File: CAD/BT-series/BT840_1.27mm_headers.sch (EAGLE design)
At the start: 64 parts, among them J1 SM02B-SRSS-TB(LF)(SN), U1 TPD4S012DRYR, U2 BT840, U3 LP5907MFX-3.3/NOPB, U4 LP5907MFX-3.3/NOPB, U5 ADS131M08IPBS, U6 BQ24072RGTR, U7 DX4R005JJ2R1800, X1 ABM3B-8.000MHZ-B2-T, X2 FC-12M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

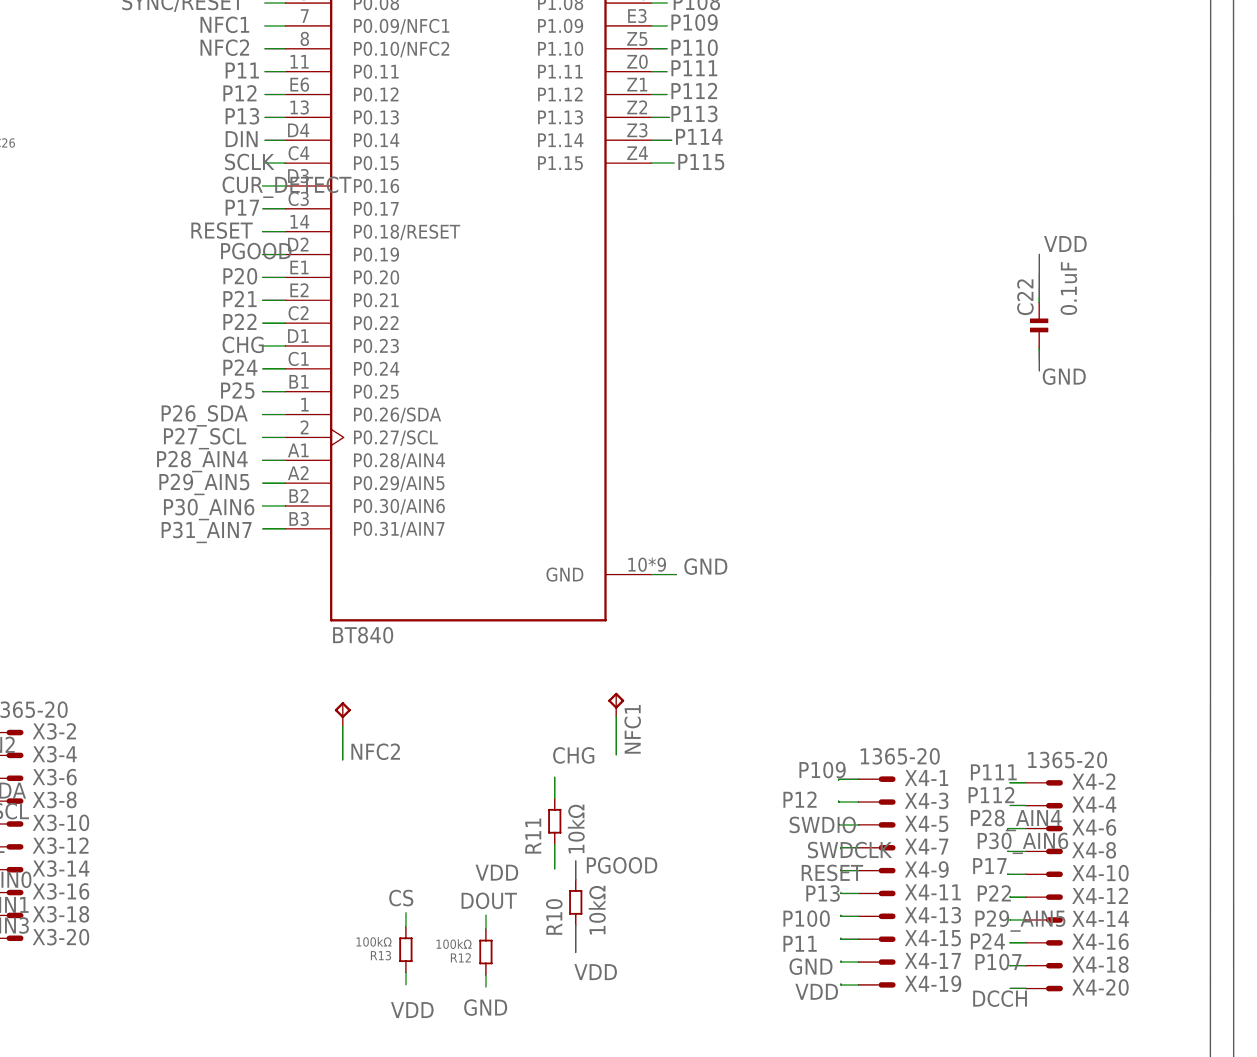
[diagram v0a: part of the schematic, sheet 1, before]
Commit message: modifed io order on bt840, some nrf52840 firmware cleanup (need to update with compass and audio too)
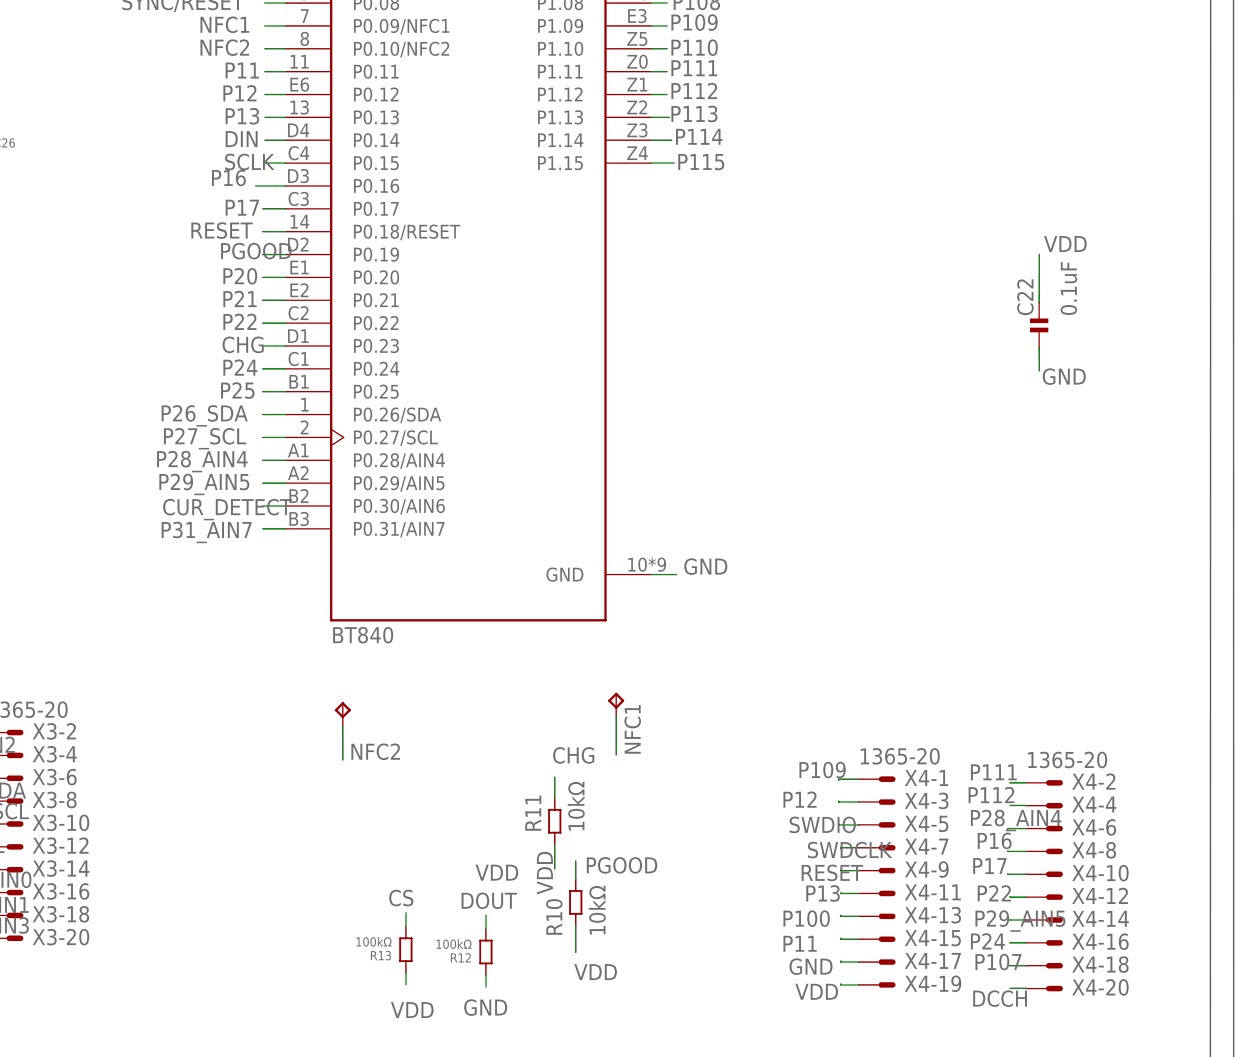
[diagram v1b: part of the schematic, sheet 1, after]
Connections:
- removed net P30_AIN6: U2.P0.30/AIN6, X4-8.S
- new net P16: U2.P0.16, X4-8.S
- net CUR_DETECT: now also U2.P0.30/AIN6; no longer U2.P0.16

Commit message: fixed cur_detect compatibility for bt40/bt840
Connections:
- removed net P29_AIN5: U2.P0.29/AIN5, X4-14.S
- new net P30_AIN6: U2.P0.30/AIN6, X4-14.S
- net CUR_DETECT: now also U2.P0.29/AIN5; no longer U2.P0.30/AIN6

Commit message: broke out the last gpio
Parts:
- added JP1: (no value), pinhead:PINHD-1X1
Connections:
- net P105: now also JP1.1
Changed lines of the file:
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@@
 <part name="X5" library="con-leotronics" library_urn="urn:adsk.eagle:library:160" deviceset="1365-16" device="" package3d_urn="urn:adsk.eagle:package:7964/1"/>
 <part name="U2" library="BT840" deviceset="BT840" device=""/>
+<part name="JP1" library="pinhead" library_urn="urn:adsk.eagle:library:325" deviceset="PINHD-1X1" device="" package3d_urn="urn:adsk.eagle:package:22485/2"/>
 </parts>
 <sheets>
@@
 <attribute name="VALUE" x="247.1419" y="68.5798" size="1.778009375" layer="96"/>
 </instance>
+<instance part="JP1" gate="G$1" x="331.724" y="147.574" smashed="yes">
+<attribute name="NAME" x="325.374" y="150.749" size="1.778" layer="95"/>
+<attribute name="VALUE" x="325.374" y="142.494" size="1.778" layer="96"/>
+</instance>
 </instances>
 <busses>
@@
 <label x="284.988" y="146.304" size="1.778" layer="95"/>
 </segment>
-</net>
+<segment>
+<pinref part="JP1" gate="G$1" pin="1"/>
+<wire x1="329.184" y1="147.574" x2="320.548" y2="147.574" width="0.1524" layer="91"/>
+<label x="316.23" y="148.082" size="1.778" layer="95"/>
+</segment>
+</net>

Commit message: update
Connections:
- removed net CLKIN: C3.1, U5.XTAL1, X1.1
- new net 8.192MHZ: C3.1, U5.XTAL1, X1.1, X3-19.S
- net CLKOUT: no longer X3-19.S
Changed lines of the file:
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@@
-</segment>
-</net>
-<net name="CLKIN" class="0">
-<segment>
-<pinref part="U5" gate="G$1" pin="XTAL1"/>
-<wire x1="439.293" y1="147.4978" x2="441.833" y2="147.4978" width="0.1524" layer="91"/>
-<label x="442.087" y="146.9898" size="1.778" layer="95"/>
-</segment>
-<segment>
-<pinref part="X1" gate="G$1" pin="1"/>
-<wire x1="481.965" y1="139.3698" x2="479.425" y2="139.3698" width="0.1524" layer="91"/>
-<label x="476.885" y="141.9098" size="1.778" layer="95"/>
-</segment>
-<segment>
-<pinref part="C3" gate="G$1" pin="1"/>
-<wire x1="471.805" y1="135.5344" x2="471.805" y2="139.3698" width="0.1524" layer="91"/>
-<label x="466.725" y="139.3698" size="1.778" layer="95"/>
 </segment>
 </net>
@@
 <label x="507.365" y="139.3698" size="1.778" layer="95"/>
 </segment>
-<segment>
-<pinref part="X3" gate="-19" pin="S"/>
-<wire x1="192.0494" y1="35.814" x2="190.5" y2="35.814" width="0.1524" layer="91"/>
-<label x="180.594" y="35.052" size="1.778" layer="95"/>
-</segment>
 </net>
 <net name="TMR" class="0">
@@
 </segment>
 </net>
+<net name="8.192MHZ" class="0">
+<segment>
+<pinref part="X3" gate="-19" pin="S"/>
+<wire x1="192.0494" y1="35.814" x2="190.5" y2="35.814" width="0.1524" layer="91"/>
+<label x="180.594" y="35.052" size="1.778" layer="95"/>
+</segment>
+<segment>
+<pinref part="U5" gate="G$1" pin="XTAL1"/>
+<wire x1="439.293" y1="147.4978" x2="441.833" y2="147.4978" width="0.1524" layer="91"/>
+<label x="442.087" y="146.9898" size="1.778" layer="95"/>
+</segment>
+<segment>
+<pinref part="X1" gate="G$1" pin="1"/>
+<wire x1="481.965" y1="139.3698" x2="479.425" y2="139.3698" width="0.1524" layer="91"/>
+<label x="476.885" y="141.9098" size="1.778" layer="95"/>
+</segment>
+<segment>
+<pinref part="C3" gate="G$1" pin="1"/>
+<wire x1="471.805" y1="135.5344" x2="471.805" y2="139.3698" width="0.1524" layer="91"/>
+<label x="466.725" y="139.3698" size="1.778" layer="95"/>
+</segment>
+</net>
